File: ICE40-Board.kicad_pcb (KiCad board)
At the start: 4 copper layers, 142.2 x 88.4 mm, 76 parts, among them Q1 2N222, SW1 SW_Push, U1 ADP1712AUJZ-3.3, U10 FT4222HQ, U2 ADP1712AUJZ-2.5, U3 ADP1712AUJZ-1.2, U4 Barrel_Jack, U5 W25X20CLSNIG, U6 USB_C_Receptacle_USB2.0, U7 ICE40HX4K-TQ144, U8 W25X20CLSNIG, U9 SIT2001BI-S2-33E-25.000000G

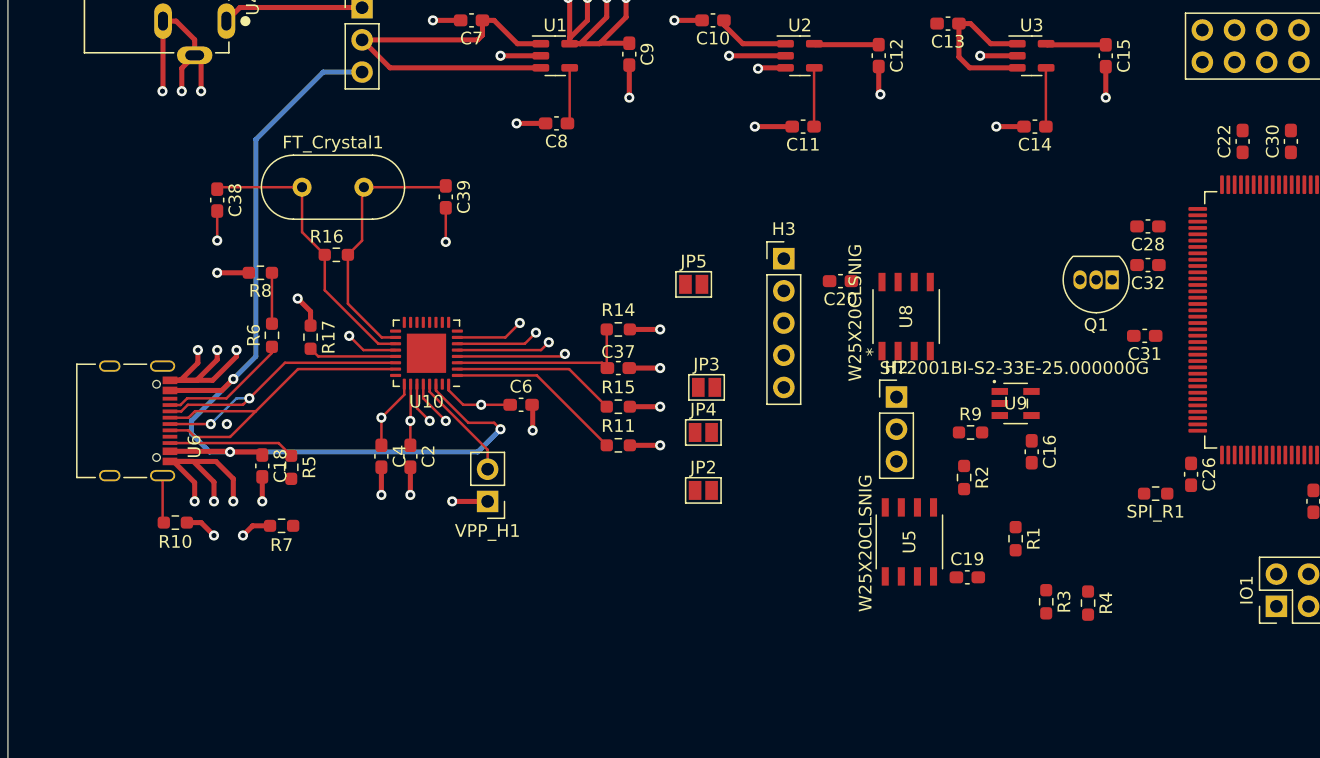
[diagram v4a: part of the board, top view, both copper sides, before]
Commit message: Routing buffers and flash
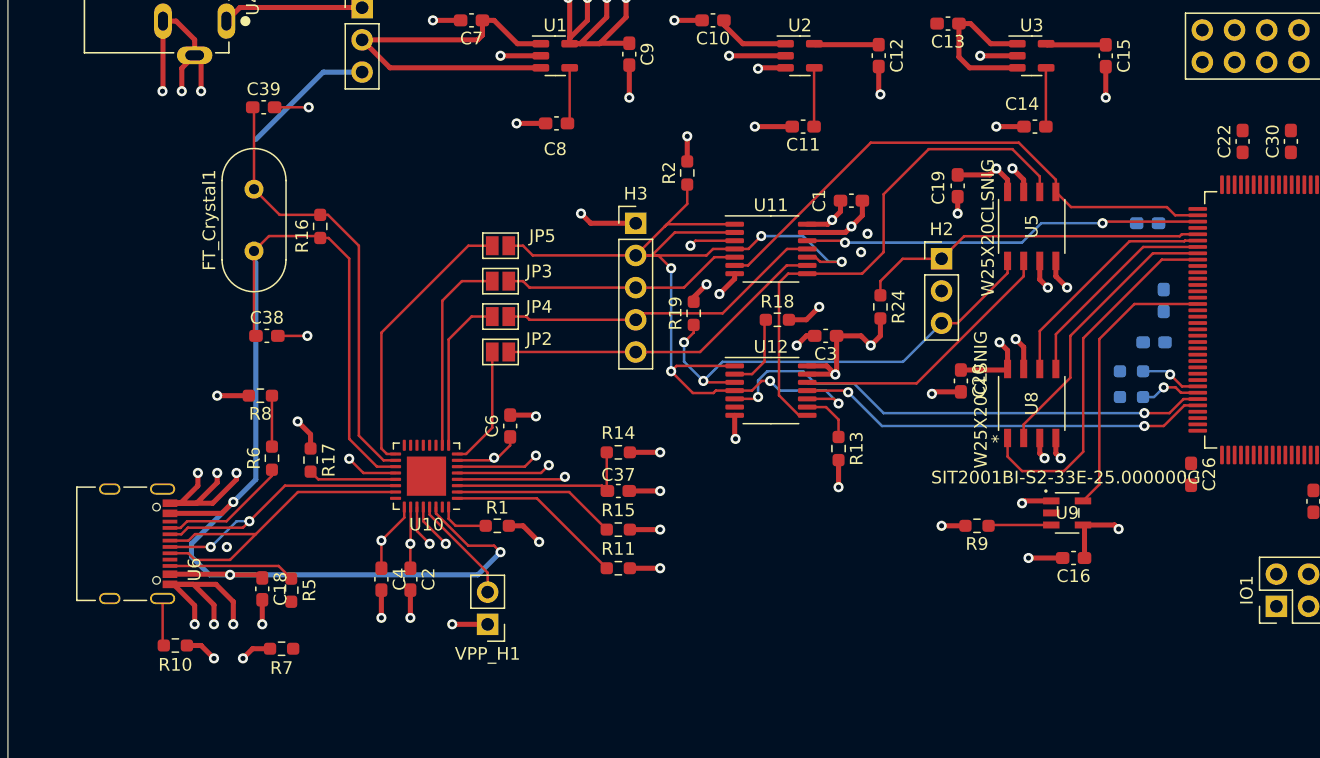
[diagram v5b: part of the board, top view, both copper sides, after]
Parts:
- removed Q1: 2N222, Package_TO_SOT_THT:TO-92_Inline
- removed SPI_R1: R, Resistor_SMD:R_0603_1608Metric_Pad0.98x0.95mm_HandSolder
- added C1: 0.1uF, Capacitor_SMD:C_0603_1608Metric_Pad1.08x0.95mm_HandSolder, F.Cu at (81.8, 35.8)
- added C3: 0.1uF, Capacitor_SMD:C_0603_1608Metric_Pad1.08x0.95mm_HandSolder, F.Cu at (79.8, 46.5)
- added R13: 10k, Resistor_SMD:R_0603_1608Metric_Pad0.98x0.95mm_HandSolder, F.Cu at (80.8, 55.4)
- added R18: 5k, Resistor_SMD:R_0603_1608Metric_Pad0.98x0.95mm_HandSolder, F.Cu at (75.9, 45.2)
- added R19: 5k, Resistor_SMD:R_0603_1608Metric_Pad0.98x0.95mm_HandSolder, F.Cu at (69.3, 44.7)
- added R24: 5k, Resistor_SMD:R_0603_1608Metric_Pad0.98x0.95mm_HandSolder, F.Cu at (84.1, 44.2)
- added U11: 74LS125, Package_SO:TSSOP-14_4.4x5mm_P0.65mm, F.Cu at (75.4, 39.6)
- added U12: 74LS126, Package_SO:TSSOP-14_4.4x5mm_P0.65mm, F.Cu at (75.4, 50.8)
- C28, C31, C32, R3, R4: moved to B.Cu
- R2: value 10k -> 5k
- moved R1 40.9 mm to (53.8, 61.5), turned to 0 degrees
- moved R2 32.5 mm to (68.8, 33.6), turned to 90 degrees
- moved C19 30.9 mm to (90.2, 34.6), turned to -90 degrees
- moved U5 26.7 mm to (96.0, 37.8)
- moved R3 19.4 mm to (103.9, 49.3), turned to 180 degrees
- moved JP2 19.4 mm to (54.1, 47.8)
- moved JP4 18.4 mm to (54.1, 45.0)
- moved JP3 18.3 mm to (54.1, 42.2)
- moved R4 16.6 mm to (103.9, 51.3), turned to 180 degrees
- moved C39 16.0 mm to (35.4, 28.4), turned to 0 degrees
- moved JP5 15.5 mm to (54.1, 39.4)
- moved C20 12.3 mm to (90.4, 50.0), turned to -90 degrees
- moved U8 12.0 mm to (96.0, 51.8)
- moved H3 12.0 mm to (64.8, 37.6)
- moved H2 11.5 mm to (88.9, 40.4)
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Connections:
- net /SS_PROG renamed /SS_PROG_BUS
- H2 pad 2: /SS -> /SS_EXT_BUS
- H2 pad 3: /SS_CONF -> /SS_FPGA_BUS
- H3 pad 2: /SS -> /SS_EXT
- H3 pad 3: /MOSI -> /MOSI_EXT
- H3 pad 4: /MISO -> /MISO_EXT
- H3 pad 5: /SCK -> /SCK_EXT
- JP2 pad 2: /SCK -> /SCK_EXT
- JP3 pad 2: /MOSI -> /MOSI_EXT
- JP4 pad 2: /MISO -> /MISO_EXT
- JP5 pad 2: /SS -> /SS_EXT
- R1 pad 1: /SCK -> Net-(R1-Pad1)
- R1 pad 2: Net-(Q1-Pad1) -> +3V3
- R2 pad 1: /SS_CONF -> /SS_EXT
- R2 pad 2: Net-(Q1-Pad1) -> +3V3
- U10 pad 32: +3V3 -> Net-(R1-Pad1)
- U5 pad 1: /SS_CONF -> /SS_FPGA_BUS
- U5 pad 2: /MISO -> /MISO_CONF
- U5 pad 5: /MOSI -> /MOSI_BUS
- U5 pad 6: /SCK -> /SCK_BUS
- U7 pad 37: /SCK -> /SCK_BUS
- U7 pad 38: /MOSI -> /MOSI_BUS
- U7 pad 39: /MISO -> /MISO_PROG
- U7 pad 67: /MOSI -> /MOSI_FPGA
- U7 pad 68: /MISO -> /MISO_FPGA
- U7 pad 70: /SCK -> /SCK_FPGA
- U7 pad 71: /SS_CONF -> /SS_FPGA
- U7 pad 72: Net-(Q1-Pad1) -> +3V3
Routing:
- net /SS_EXT: track 0.00 -> 86.9 mm, vias 0 -> 6
- net +3V3: track 74.4 -> 125.3 mm, vias 14 -> 29
- net /MOSI_BUS: track 0.00 -> 43.5 mm
- net /SCK_BUS: track 0.00 -> 41.5 mm
- net /MOSI_FPGA: track 0.00 -> 40.6 mm, vias 0 -> 2
- net /SS_FPGA_BUS: track 0.00 -> 36.4 mm, vias 0 -> 2
- net VBUS: track 81.3 -> 115.3 mm
- net /MISO_FPGA: track 0.00 -> 32.6 mm, vias 0 -> 2
- net /MISO_PROG: track 0.00 -> 31.6 mm, vias 0 -> 2
- net GND: track 124.4 -> 153.9 mm, vias 37 -> 50
- net Net-(U7-Pad45): track 0.00 -> 29.1 mm
- net /SS_PROG_BUS: track 0.00 -> 27.7 mm
- net /SCK_EXT: track 0.00 -> 26.4 mm
- net /MISO_EXT: track 0.00 -> 26.0 mm
- net Net-(C38-Pad1): track 23.0 -> 0.00 mm
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
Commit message: everything routed just IO pins remaining
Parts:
- C33, C34, R12: moved to B.Cu
- U5, U8: footprint W25X20CLSNIG:W25X20CLSNIG -> Package_SO:SOIC-8_3.9x4.9mm_P1.27mm
- U9: footprint SIT2001BC-S2-33E-25.0:SIT2001BC-S2-33E-25.0 -> Package_TO_SOT_SMD:SOT-23-5_HandSoldering
- moved IO1 202.2 mm to (-85.9, 87.9)
- moved IO2 169.8 mm to (-12.0, 98.3)
- moved IO3 161.6 mm to (-0.27, 113.2)
- moved SW1 35.8 mm to (136.4, 58.5)
- moved R18 28.1 mm to (101.9, 56.1)
- moved R12 21.1 mm to (120.4, 41.1)
- moved C33 18.5 mm to (126.2, 41.1), turned to 90 degrees
- moved R24 18.4 mm to (98.0, 32.3), turned to 180 degrees
- moved C19 17.8 mm to (85.6, 51.8)
- moved C34 17.6 mm to (123.2, 41.1), turned to 90 degrees
- moved C38 16.5 mm to (22.0, 37.2), turned to -90 degrees
- moved R19 16.3 mm to (85.3, 41.4)
- moved C20 16.0 mm to (87.9, 34.3), turned to 90 degrees
- moved U9 13.5 mm to (104.1, 48.0)
- moved C16 13.2 mm to (104.4, 51.8)
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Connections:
- H3 pad 4: /MISO_EXT -> /MISO
- JP4 pad 2: /MISO_EXT -> /MISO
- U11 pad 11: /MISO_EXT -> /MISO
- U12 pad 11: /MISO_FPGA -> /MISO
- U7 pad 68: /MISO_FPGA -> /MISO
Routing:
- net +1V2: track 4.74 -> 176.2 mm, vias 0 -> 9
- net +2V5: track 18.0 -> 86.7 mm, vias 0 -> 2
- net GND: track 153.9 -> 217.4 mm, vias 50 -> 71
- net /MISO: track 0.00 -> 52.8 mm, vias 0 -> 2
- net VBUS: track 115.3 -> 63.3 mm
- net +3V3: track 125.3 -> 171.1 mm, vias 29 -> 36
- net /SS_FPGA: track 6.11 -> 51.0 mm, vias 0 -> 2
- net Net-(R4-Pad1): track 4.80 -> 48.5 mm, vias 1 -> 2
- net /SCK_FPGA: track 4.25 -> 37.1 mm
- net /MISO_FPGA: track 32.6 -> 0.00 mm, vias 2 -> 0
- net Net-(C38-Pad1): track 0.00 -> 31.0 mm
- net /GND_PLL1: track 0.00 -> 30.8 mm, vias 0 -> 1
- net /VCC_PLL1: track 0.00 -> 30.2 mm, vias 0 -> 1
- net /MISO_EXT: track 26.0 -> 0.00 mm
- net Net-(U7-Pad52): track 22.2 -> 5.73 mm
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
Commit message: previous commit message incorrect, this commit has fully routed design except IO
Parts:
- C3: moved to B.Cu
- moved IO1 192.3 mm to (106.4, 88.4)
- moved IO3 183.4 mm to (173.5, 54.5)
- moved IO2 181.8 mm to (142.2, 2.03)
- moved C3 4.68 mm to (83.8, 54.9), turned to -90 degrees
- moved U9 3.97 mm to (101.6, 45.0)
- moved C20 2.62 mm to (85.6, 35.6)
- moved C16 1.63 mm to (103.4, 50.5), turned to -90 degrees
- moved C19 1.55 mm to (85.9, 53.3)
- moved R9 1.37 mm to (98.0, 50.8), turned to -90 degrees
- moved C1 1.02 mm to (79.2, 33.8)
- moved R4 0.84 mm to (99.1, 52.1)
- moved R3 0.80 mm to (99.1, 48.8)
- moved R19 0.25 mm to (85.1, 41.4)
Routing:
- net /MISO: track 52.8 -> 94.1 mm, vias 2 -> 4
- net /MOSI_BUS: track 34.3 -> 67.3 mm, vias 0 -> 2
- net /SCK_BUS: track 39.9 -> 59.5 mm, vias 0 -> 2
- net +3V3: track 171.1 -> 182.3 mm, vias 36 -> 39
- net /SS_EXT_BUS: track 20.1 -> 27.9 mm
- net Net-(U7-Pad45): track 29.5 -> 36.5 mm
- net GND: track 217.4 -> 224.1 mm, vias 71 -> 72
- net Net-(U7-Pad44): track 25.3 -> 32.1 mm
- net /MISO_PROG: track 29.9 -> 34.3 mm
- net Net-(U7-Pad43): track 20.7 -> 25.0 mm
- net Net-(U7-Pad42): track 22.2 -> 26.4 mm
- net /SS_EXT: track 92.4 -> 94.3 mm
- net Net-(R9-Pad1): track 3.92 -> 5.70 mm
- net Net-(R4-Pad1): track 48.5 -> 49.4 mm
- net Net-(R3-Pad1): track 14.1 -> 14.9 mm
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
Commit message: No DRC errors, board fully routed
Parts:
- IO3: value Conn_02x09_Row_Letter_Last -> Conn_02x13_Row_Letter_Last; footprint Connector_PinHeader_2.00mm:PinHeader_2x09_P2.00mm_Vertical -> Connector_PinHeader_2.54mm:PinHeader_2x13_P2.54mm_Vertical
- moved IO2 34.4 mm to (114.2, 22.0), turned to 90 degrees
- moved SW1 32.8 mm to (103.7, 59.9)
- moved IO3 22.6 mm to (151.9, 61.3)
- moved IO1 18.1 mm to (114.2, 72.0)
- moved C21 12.1 mm to (137.7, 31.2), turned to 0 degrees
- moved C23 7.10 mm to (131.8, 61.2)
- moved C34 7.10 mm to (130.3, 41.1)
- moved C22 7.10 mm to (119.9, 29.5)
- moved C24 7.10 mm to (125.5, 61.2)
- moved C30 7.10 mm to (122.7, 29.5)
- moved R12 7.10 mm to (127.5, 41.1)
- moved U7 7.10 mm to (126.9, 45.2)
- moved C29 7.10 mm to (128.1, 61.2)
- moved C33 7.10 mm to (133.3, 41.1)
- moved C25 6.98 mm to (135.6, 61.0)
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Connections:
- IO2 pad 10: /29b -> /33b
- IO2 pad 11: /28a -> /32a
- IO2 pad 12: /28b -> /32b
- IO2 pad 13: /27a -> /31a
- IO2 pad 14: /27b -> /31b
- IO2 pad 15: /26a -> /30a
- IO2 pad 16: /26b -> /30b
- IO2 pad 17: /25a -> /29a
- IO2 pad 18: /25b -> /29b
- IO2 pad 19: /24a -> /28a
- IO2 pad 20: /24b -> /28b
- IO2 pad 21: /23a -> /27a
- IO2 pad 22: /23b -> /27b
- IO2 pad 23: /22a -> /26a
- IO2 pad 24: /22b -> /26b
- IO2 pad 25: /21a -> /25a
- IO2 pad 26: /21b -> /25b
- IO2 pad 3: /32a -> /36a
- IO2 pad 4: /32b -> /36b
- IO2 pad 5: /31a -> /35a
- IO2 pad 6: /31b -> /35b
- IO2 pad 7: /30a -> /34a
- IO2 pad 8: /30b -> /34b
- IO2 pad 9: /29a -> /33a
- IO3 pad 1: GND -> +3V3
- IO3 pad 10: /17b -> /16a
- IO3 pad 11: /16a -> /17b
- IO3 pad 12: /16b -> /17a
- IO3 pad 13: /15a -> /18b
- IO3 pad 14: /15b -> /18a
- IO3 pad 15: /14a -> /19b
- IO3 pad 16: /14b -> /19a
- IO3 pad 17: /13a -> /20b
- IO3 pad 18: /13b -> /20a
- IO3 pad 2: +3V3 -> GND
- IO3 pad 3: /20a -> /13b
- IO3 pad 4: /20b -> /13a
- IO3 pad 5: /19a -> /14b
- IO3 pad 6: /19b -> /14a
- IO3 pad 7: /18a -> /15b
- IO3 pad 8: /18b -> /15a
- IO3 pad 9: /17a -> /16b
- U7 pad 10: /31a -> /26b
- U7 pad 11: /30b -> /27a
- U7 pad 114: unconnected-(U7-Pad114) -> /13a
- U7 pad 115: unconnected-(U7-Pad115) -> /13b
- U7 pad 116: unconnected-(U7-Pad116) -> /14a
- U7 pad 117: unconnected-(U7-Pad117) -> /14b
- U7 pad 118: unconnected-(U7-Pad118) -> /15a
- U7 pad 119: unconnected-(U7-Pad119) -> /15b
- U7 pad 12: /30a -> /27b
- U7 pad 120: unconnected-(U7-Pad120) -> /16a
- U7 pad 121: unconnected-(U7-Pad121) -> /16b
- U7 pad 122: /20b -> /17a
- U7 pad 124: /20a -> /17b
- U7 pad 125: /19b -> /18a
- U7 pad 128: /19a -> /18b
- U7 pad 129: /18b -> /19a
- U7 pad 130: /18a -> /19b
- U7 pad 134: /17b -> /20a
- U7 pad 135: /17a -> /20b
- U7 pad 136: /16b -> /21a
- U7 pad 137: /16a -> /21b
- U7 pad 138: /15b -> /22a
- U7 pad 139: /15a -> /22b
- U7 pad 141: /14b -> /23a
- U7 pad 142: /14a -> /23b
- U7 pad 143: /13b -> /24a
- U7 pad 144: /13a -> /24b
- U7 pad 15: /29b -> /28a
- U7 pad 16: /29a -> /28b
- U7 pad 17: /28b -> /29a
- U7 pad 18: /28a -> /29b
- U7 pad 19: /27b -> /30a
- U7 pad 20: /27a -> /30b
- U7 pad 21: /26b -> /31a
- U7 pad 22: /26a -> /31b
- U7 pad 23: /25b -> /32a
- U7 pad 24: /25a -> /32b
- U7 pad 25: /24b -> /33a
- U7 pad 26: /24a -> /33b
- U7 pad 28: /23b -> /34a
- U7 pad 29: /23a -> /34b
- U7 pad 31: /22b -> /35a
- U7 pad 32: /22a -> /35b
- U7 pad 33: /21b -> /36a
- U7 pad 34: /21a -> /36b
- U7 pad 7: /32b -> /25a
- U7 pad 8: /32a -> /25b
- U7 pad 9: /31b -> /26a
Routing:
- net /12b: track 0.00 -> 43.7 mm, vias 0 -> 1
- net +1V2: track 176.6 -> 213.2 mm
- net GND: track 224.1 -> 251.2 mm, vias 72 -> 78
- net /11a: track 0.00 -> 26.7 mm, vias 0 -> 1
- net /10a: track 0.00 -> 25.9 mm, vias 0 -> 1
- net /12a: track 0.00 -> 25.5 mm, vias 0 -> 1
- net /9a: track 0.00 -> 25.4 mm, vias 0 -> 1
- net /8a: track 0.00 -> 25.1 mm, vias 0 -> 1
- net /25b: track 0.00 -> 25.0 mm, vias 0 -> 1
- net /28b: track 0.00 -> 24.4 mm, vias 0 -> 1
- net +3V3: track 182.3 -> 206.7 mm, vias 39 -> 42
- net /26b: track 0.00 -> 24.2 mm, vias 0 -> 1
- net /27b: track 0.00 -> 24.1 mm, vias 0 -> 1
- net /7a: track 0.00 -> 24.0 mm, vias 0 -> 1
- net /29b: track 0.00 -> 23.8 mm, vias 0 -> 1
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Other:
- board size 142.2 x 88.4 mm -> 134.4 x 58 mm
